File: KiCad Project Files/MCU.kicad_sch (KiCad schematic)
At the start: 25 parts, among them SW1 Boot, SW2 Reset, U1 RP2040, U2 W25Q128JVS, Y1 12MHz

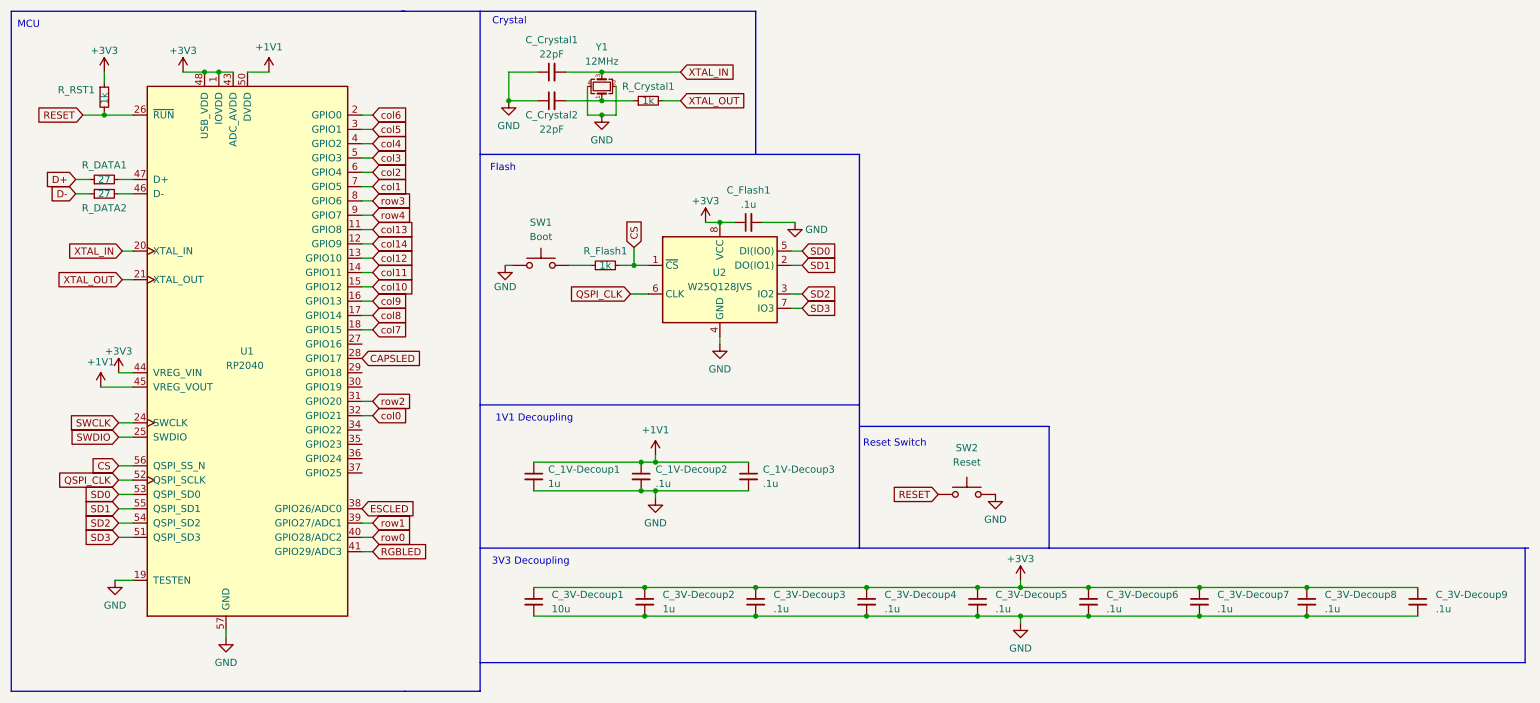
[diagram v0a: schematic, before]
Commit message: begin work on stm32 branch
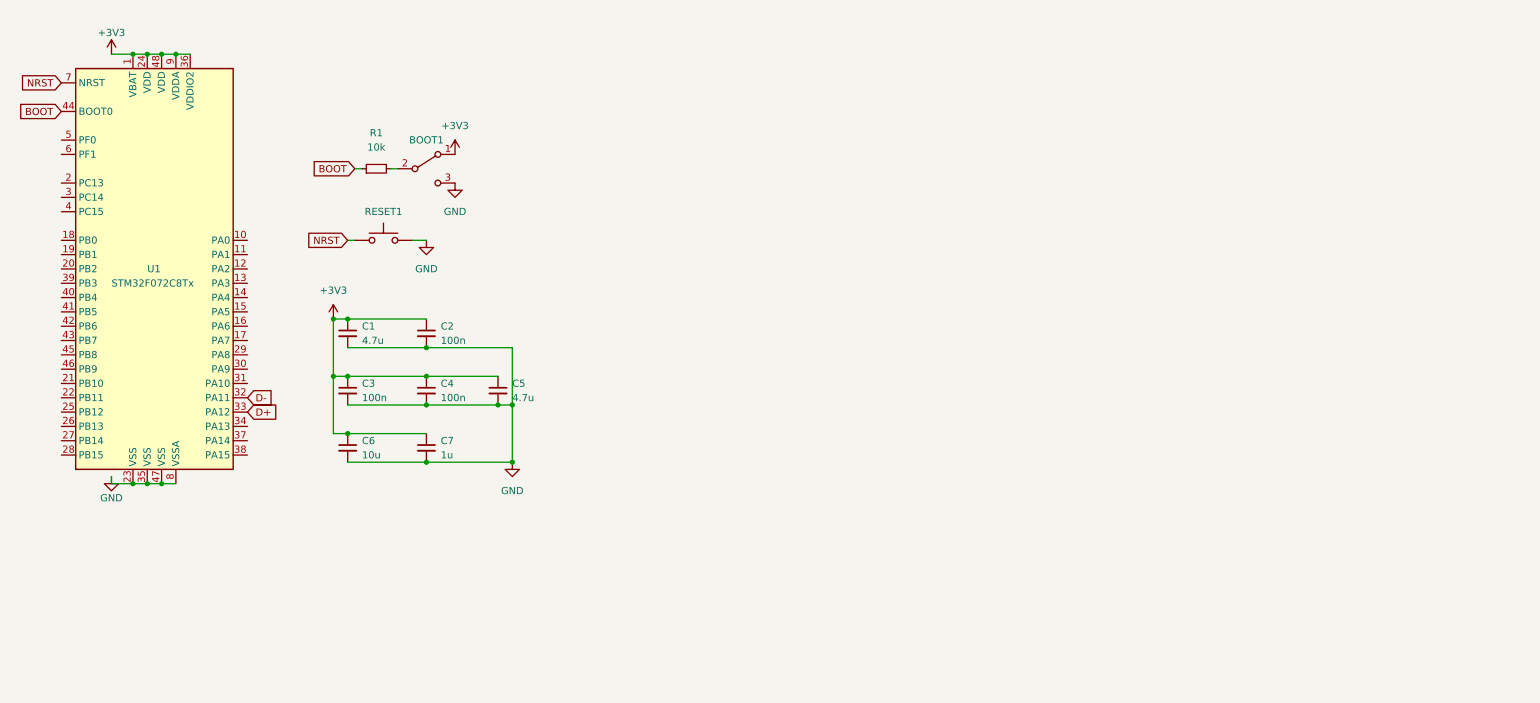
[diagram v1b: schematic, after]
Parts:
- removed C_1V-Decoup1, C_3V-Decoup2: 1u, Capacitor_SMD:C_0402_1005Metric, symbol Device:C_Small
- removed C_1V-Decoup2, C_1V-Decoup3, C_3V-Decoup3, C_3V-Decoup4, C_3V-Decoup5, C_3V-Decoup6, C_3V-Decoup7, C_3V-Decoup8, C_3V-Decoup9, C_Flash1: .1u, Capacitor_SMD:C_0402_1005Metric, symbol Device:C_Small
- removed C_3V-Decoup1: 10u, Capacitor_SMD:C_0402_1005Metric, symbol Device:C_Small
- removed C_Crystal1, C_Crystal2: 22pF, Capacitor_SMD:C_0402_1005Metric, symbol Device:C_Small
- removed R_Crystal1, R_Flash1, R_RST1: 1k, Resistor_SMD:R_0402_1005Metric, symbol Device:R_Small
- removed R_DATA1, R_DATA2: 27, Resistor_SMD:R_0402_1005Metric, symbol Device:R_Small
- removed SW1: Boot, Button_Switch_SMD:SW_SPST_TL3342, symbol Switch:SW_Push
- removed SW2: Reset, Button_Switch_SMD:SW_SPST_TL3342, symbol Switch:SW_Push
- removed U1: RP2040, cipulot_parts:RP2040-QFN-56, symbol cipulot_parts:RP2040
- removed U2: W25Q128JVS, Package_SO:SOIC-8_5.23x5.23mm_P1.27mm, symbol Memory_Flash:W25Q128JVS
- removed Y1: 12MHz, Crystal:Crystal_SMD_3225-4Pin_3.2x2.5mm, symbol Device:Crystal_GND24_Small
- added BOOT1: SW_SPDT, Button_Switch_SMD:SW_SPDT_PCM12, symbol Switch:SW_SPDT
- added C1, C5: 4.7u, Capacitor_SMD:C_0402_1005Metric, symbol Device:C_Small
- added C2, C3, C4: 100n, Capacitor_SMD:C_0402_1005Metric, symbol Device:C_Small
- added C6: 10u, Capacitor_SMD:C_0402_1005Metric, symbol Device:C_Small
- added C7: 1u, Capacitor_SMD:C_0402_1005Metric, symbol Device:C_Small
- added R1: 10k, Resistor_SMD:R_0402_1005Metric, symbol Device:R_Small
- added RESET1: SW_Push, Button_Switch_SMD:SW_SPST_TL3342, symbol Switch:SW_Push
- added U1: STM32F072C8Tx, Package_QFP:LQFP-48_7x7mm_P0.5mm, symbol MCU_ST_STM32F0:STM32F072C8Tx
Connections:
- net +3V3: now also BOOT1.1 (A), C1.1, C2.1, C3.1, C4.1, C5.1, C6.1, C7.1, U1.1 (VBAT), U1.24 (VDD), U1.36 (VDDIO2), U1.48 (VDD), U1.9 (VDDA)
- net D+: now also U1.33 (PA12)
- net D-: now also U1.32 (PA11)
- net GND: now also BOOT1.3 (C), C1.2, C2.2, C3.2, C4.2, C5.2, C6.2, C7.2, RESET1.2, U1.23 (VSS), U1.35 (VSS), U1.47 (VSS), U1.8 (VSSA)
- new net: BOOT1.2 (B), R1.2
- new net BOOT: R1.1, U1.44 (BOOT0)
- new net NRST: RESET1.1, U1.7 (NRST)
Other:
- note removed: "1V1 Decoupling"
- note removed: "3V3 Decoupling"
- note removed: "Crystal"
- note removed: "Flash"
- note removed: "MCU"
- note removed: "Reset Switch"
